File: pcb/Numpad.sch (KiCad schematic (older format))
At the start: 61 parts, among them P1 USB-MICRO-B, P2 HOLE, P3 HOLE, P4 HOLE, P5 HOLE, SW1 F13, SW10 8, SW11 9, SW12 PLUS, SW13 4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

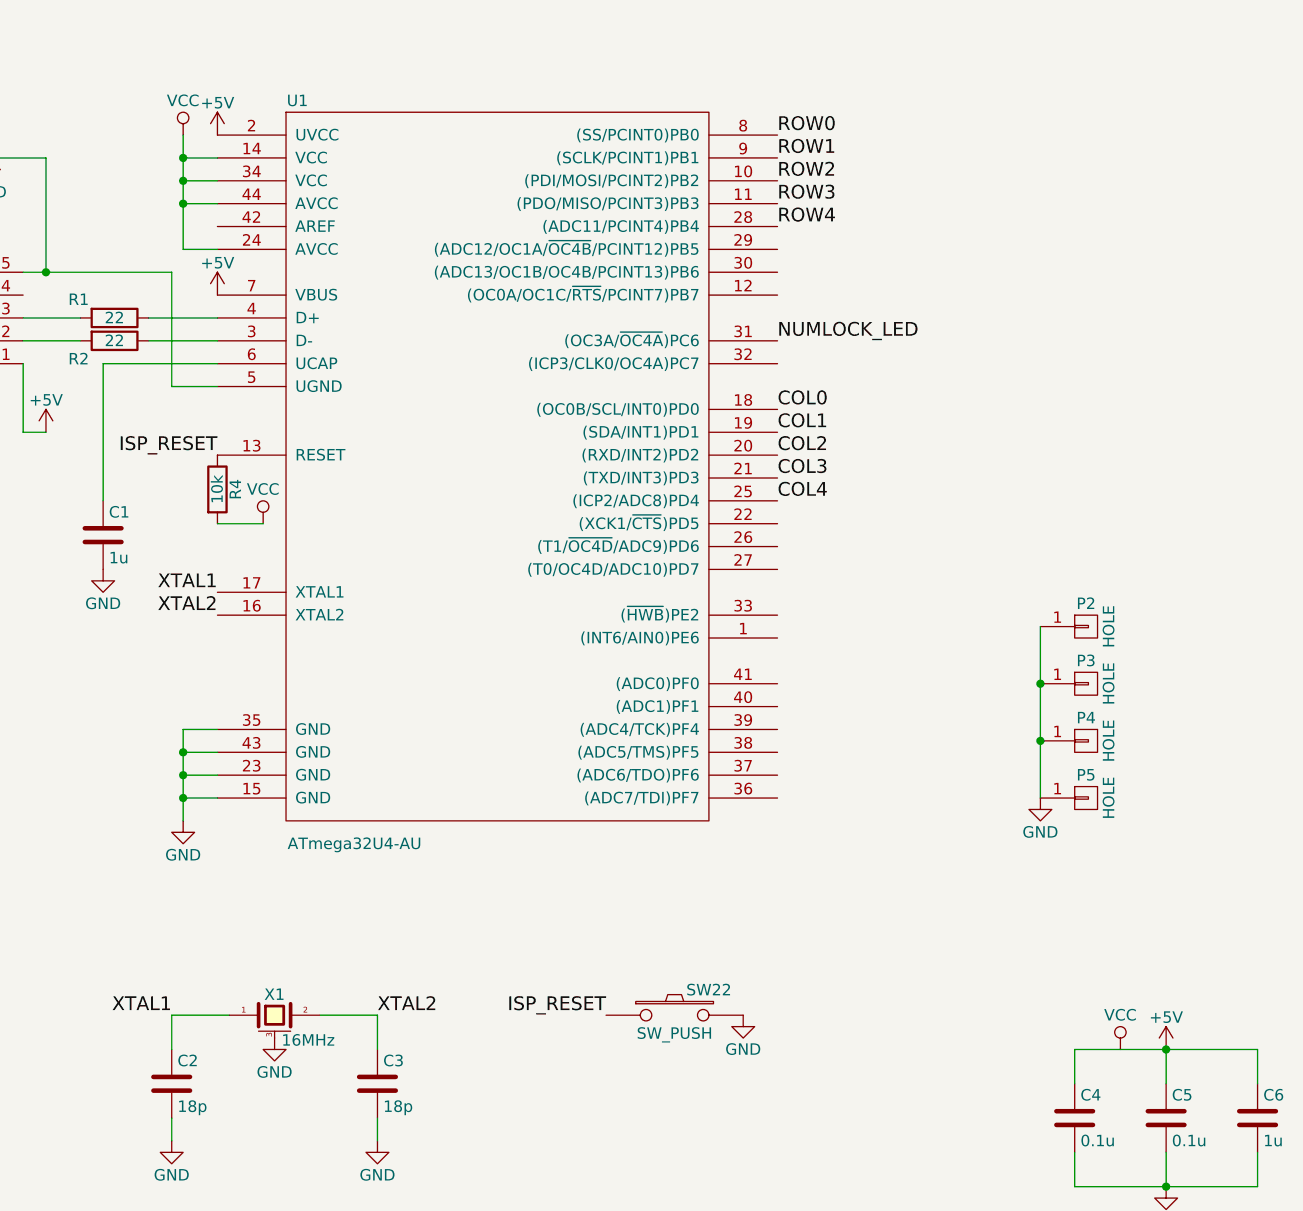
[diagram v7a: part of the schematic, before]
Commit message: Fix VCC/+5V problem. Shrink board by like 10 mils
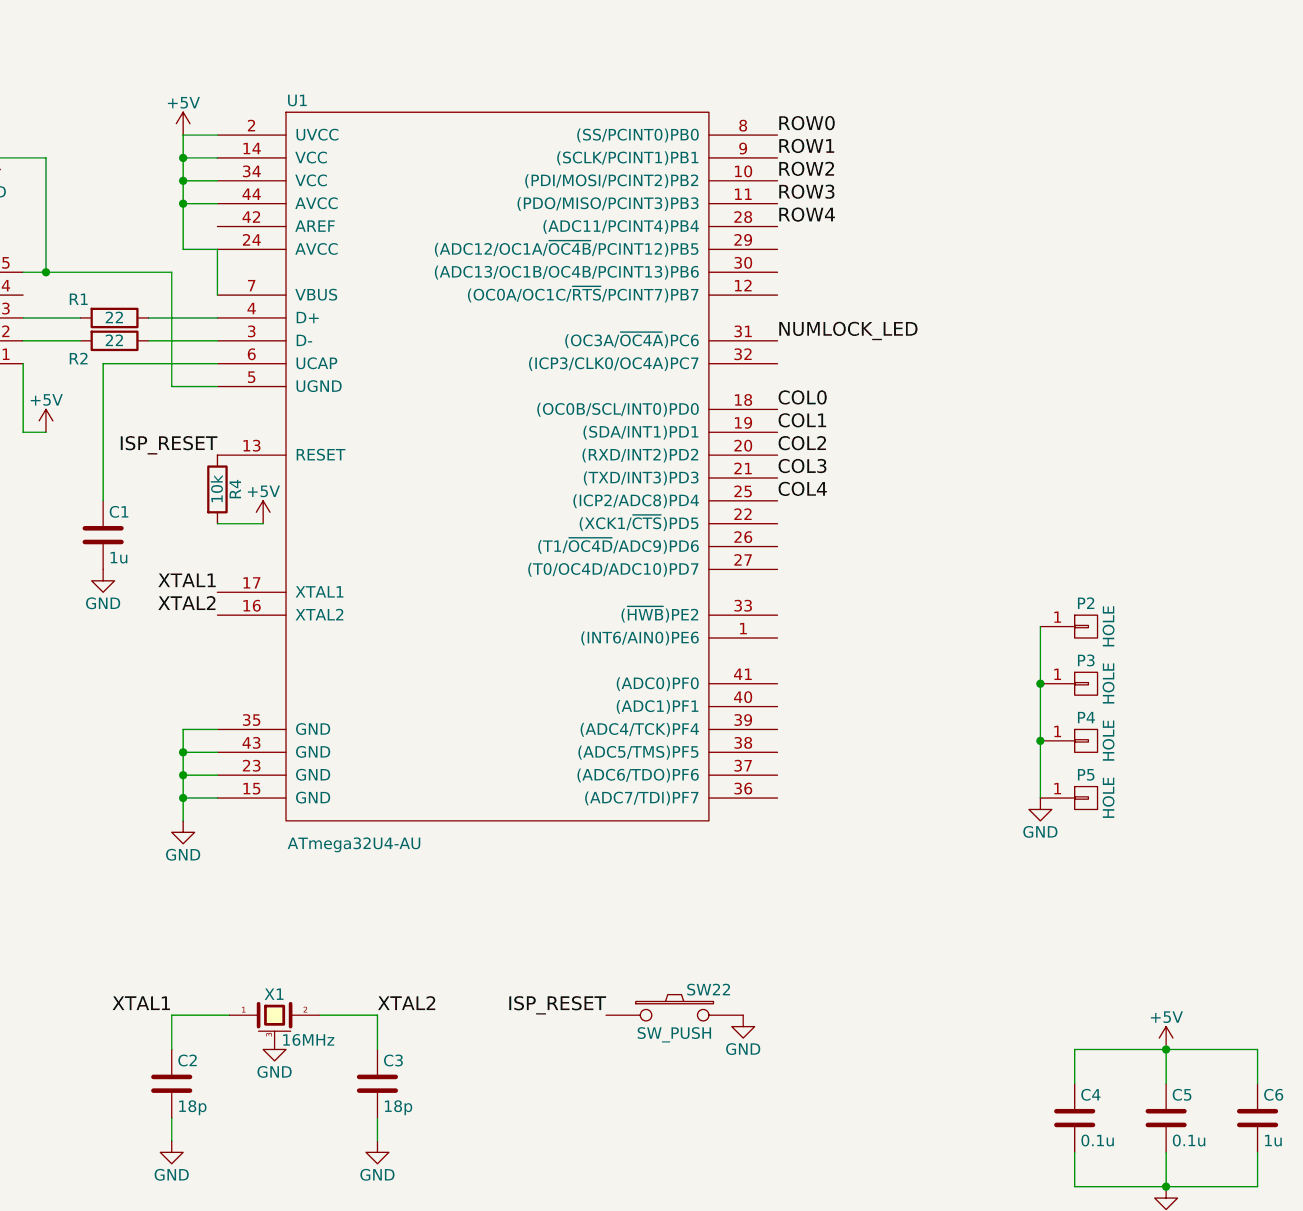
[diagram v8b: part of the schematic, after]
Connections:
- net VCC is gone; now on net +5V: R4.2, U1.14 (VCC), U1.24 (AVCC), U1.34 (VCC), U1.44 (AVCC)
